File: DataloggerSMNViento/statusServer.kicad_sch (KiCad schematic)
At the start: 15 parts, among them Q1 2N7000, Q2 2N7000, Q3 2N7000

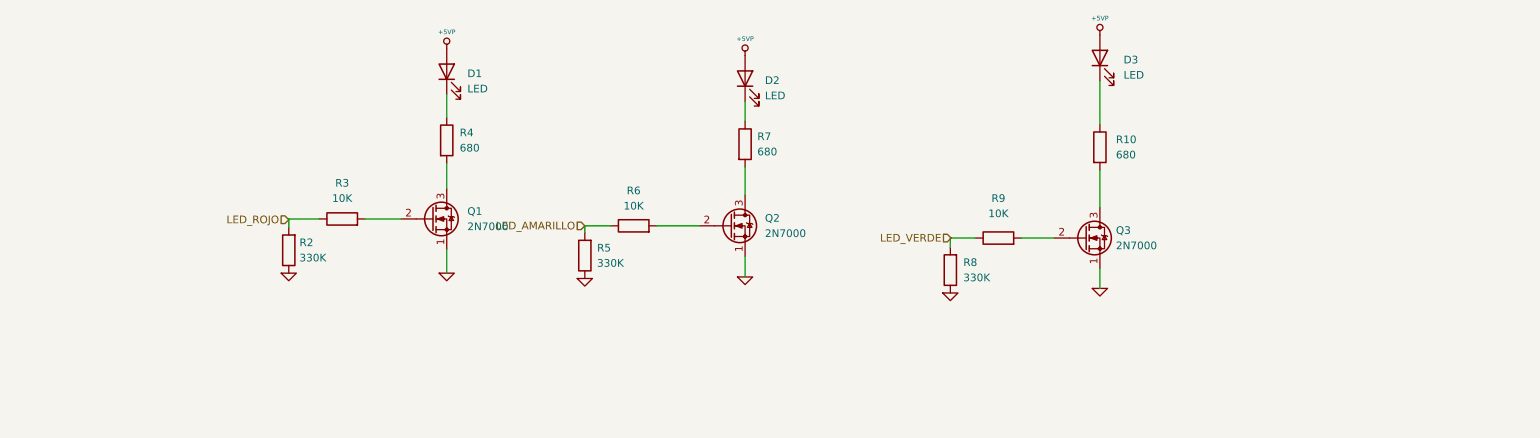
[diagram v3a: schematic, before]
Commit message: Subo la version v1.2 THT de la poncho, para fabricar en el SMN
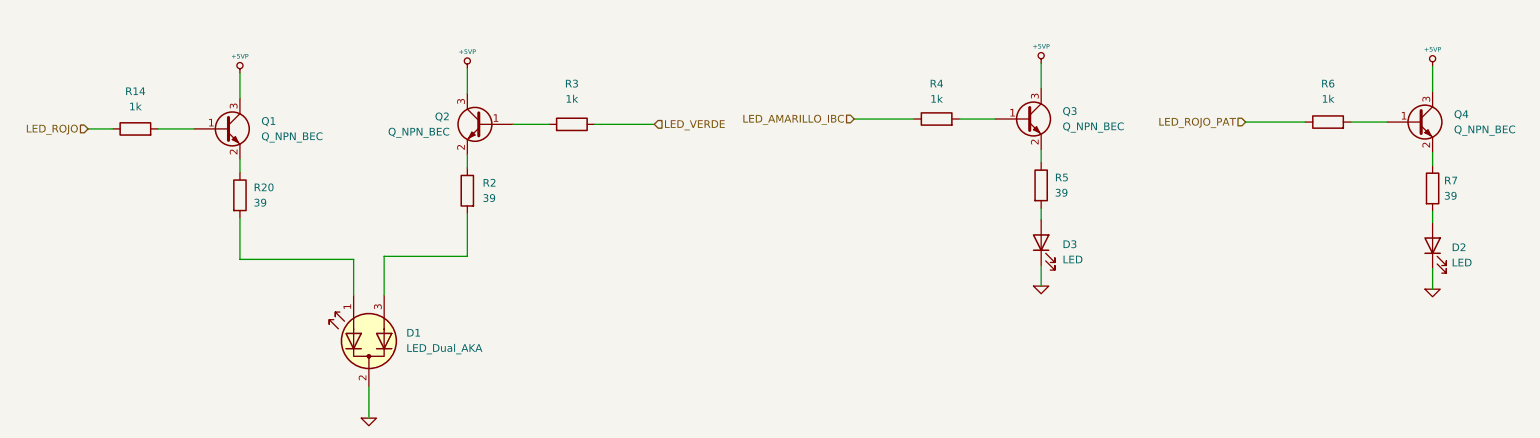
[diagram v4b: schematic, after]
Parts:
- removed D1, D3: LED, LED_SMD:LED_1206_3216Metric, symbol Device:LED
- removed Q1, Q2, Q3: 2N7000, Package_TO_SOT_SMD:SOT-23, symbol Transistor_FET:2N7000
- removed R10: 680, Resistor_SMD:R_1206_3216Metric, symbol Device:R
- removed R8: 330K, Resistor_SMD:R_1206_3216Metric, symbol Device:R
- removed R9: 10K, Resistor_SMD:R_1206_3216Metric, symbol Device:R
- added D1: LED_Dual_AKA, LED_THT:LED_D3.0mm-3, symbol Device:LED_Dual_AKA
- added D2: LED, LED_THT:LED_D3.0mm, symbol Device:LED
- added Q1, Q2, Q3, Q4: Q_NPN_BEC, Package_TO_SOT_SMD:SOT-23, symbol Device:Q_NPN_BEC
- added R14: 1k, Resistor_SMD:R_1206_3216Metric, symbol Device:R
- added R20: 39, Resistor_SMD:R_1206_3216Metric, symbol Device:R
- D3: renamed from D2; footprint LED_SMD:LED_1206_3216Metric -> LED_THT:LED_D3.0mm
- R2, R5: value 330K -> 39
- R3, R6: value 10K -> 1k
- R4: value 680 -> 1k
- R7: value 680 -> 39
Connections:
- net +5VP: now also Q1.3 (C), Q2.3 (C), Q3.3 (C), Q4.3 (C); no longer D3.2 (A)
- net GND: now also D3.1 (K), D1.2 (K), D2.1 (K); no longer R2.1, R5.1
- net LED_ROJO: now also R14.1; no longer R2.2, R3.1
- net LED_VERDE: now also R3.1
- net at R3.2: now also Q2.1 (B)
- net at R4.2: now also Q3.1 (B)
- net at R7.1: now also Q4.2 (E); no longer D3.1 (K)
- net at R7.2: now also D2.2 (A)
- net LED_AMARILLO_IBC: now reaches R4.1
- net at R6.2: now also Q4.1 (B)
- net LED_AMARILLO: no longer names the net of R5.2
- net LED_AMARILLO: now also D3.2 (A); no longer R6.1
- new net: Q3.2 (E), R5.1
- new net: Q1.1 (B), R14.2
- new net: Q1.2 (E), R20.1
- new net: D1.1 (A1), R20.2
- new net: D1.3 (A2), R2.2
- new net: Q2.2 (E), R2.1
- new net LED_ROJO_PAT: R6.1
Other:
- moved on the sheet: D3
